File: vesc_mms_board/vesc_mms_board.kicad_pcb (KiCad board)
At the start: 2 copper layers, 60 x 104.5 mm, 51 parts, among them J1 RJ45_LED_Shielded, J2 RJ45_LED_Shielded, J3 Conn_01x04, J4 Conn_01x05, J5 VCC_IN, J6 Conn_01x02, SW1 SW_DIP_x02, U1 CH334R, Y1 12Mhz

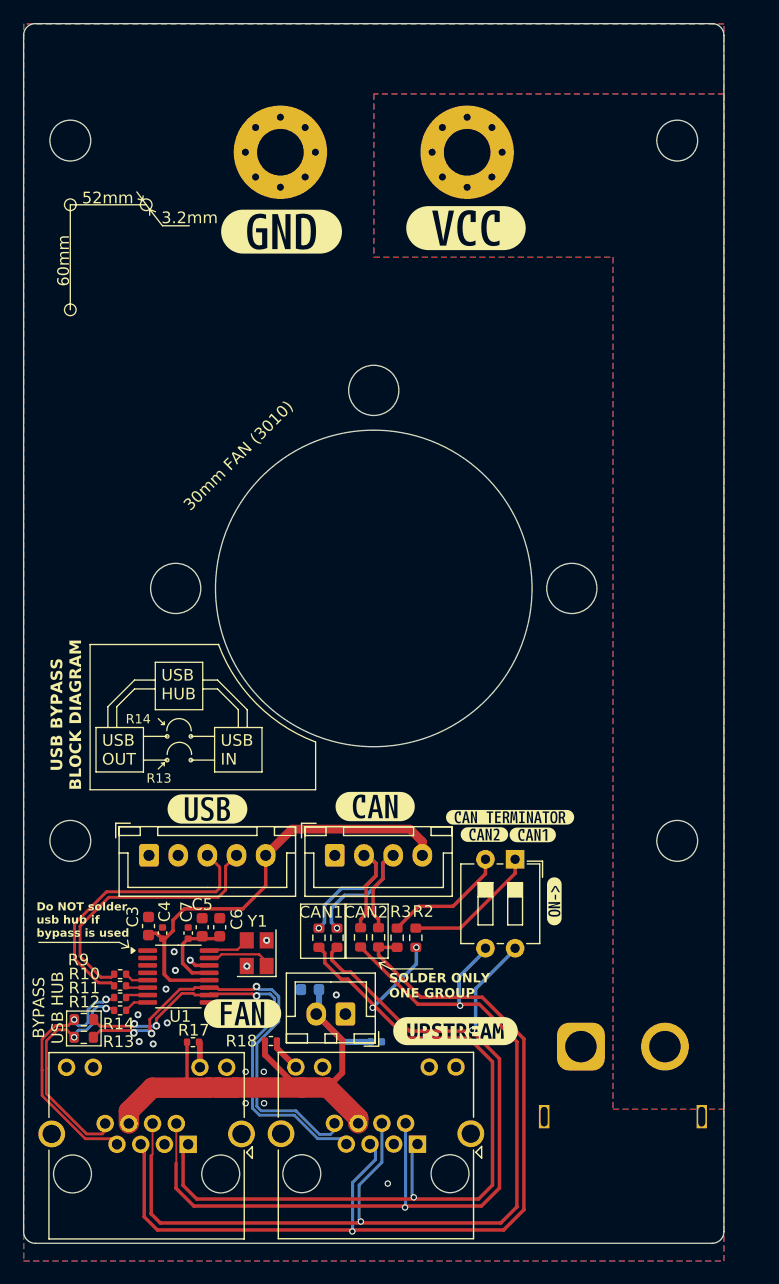
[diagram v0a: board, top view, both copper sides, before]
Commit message: fixed xt60 connvetor
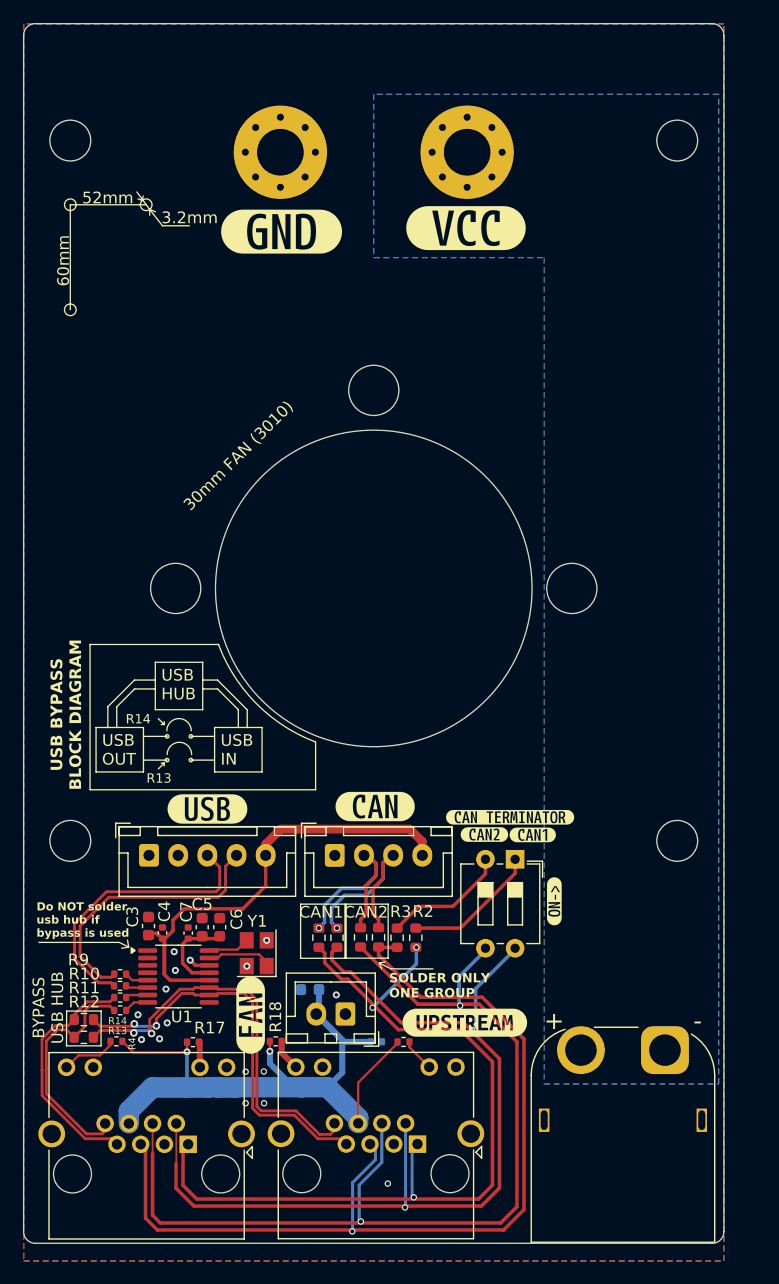
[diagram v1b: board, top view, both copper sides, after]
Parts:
- added R1: 1k, Resistor_SMD:R_0402_1005Metric, F.Cu at (112.5, 131.2)
- added R4: 1k, Resistor_SMD:R_0402_1005Metric, F.Cu at (88.0, 131.2)
- J5: moved to F.Cu
- moved J5 7.21 mm to (134.9, 131.9), turned to 180 degrees
- moved kibuzzard-6754762D 1.08 mm to (117.8, 129.6)
- moved kibuzzard-674E4631 0.70 mm to (99.5, 128.9), turned to 90 degrees
- moved R18 0.41 mm to (101.6, 131.2)
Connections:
- J1 pad 10: unconnected-(J1-Pad10) -> Net-(J1-Pad10)
- J1 pad 9: unconnected-(J1-Pad9) -> GND
- J2 pad 11: unconnected-(J2-Pad11) -> GND
- J2 pad 12: unconnected-(J2-Pad12) -> Net-(J2-Pad12)
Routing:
- net +12V: track 48.1 -> 62.3 mm, vias 0 -> 2
- net Net-(J2-Pad12): track 0.00 -> 4.87 mm
- net USB_UPSTREAM_D+: track 38.1 -> 35.0 mm, vias 3 -> 2
- net USB_UPSTREAM_D-: track 37.3 -> 34.4 mm, vias 3 -> 2
- net Net-(J1-Pad10): track 0.00 -> 2.75 mm
- net USB_DOWNSTREAM_D-: track 21.8 -> 21.1 mm, vias 2 -> 0
- net +5V: track 41.8 -> 42.3 mm
- net USB_DOWNSTREAM_D+: track 20.0 -> 20.5 mm, vias 2 -> 0
- removed copper zone on F.Cu, net VCC

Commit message: added gerber files
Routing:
- net GND: vias 16 -> 404

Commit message: added gerber files
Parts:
- C1, C2: moved to F.Cu
- moved R1 11.7 mm to (101.2, 128.8), turned to -90 degrees
- moved C2 10.2 mm to (103.0, 123.9), turned to -90 degrees
- moved C1 4.37 mm to (101.8, 123.3), turned to -90 degrees
- moved Y1 0.68 mm to (99.3, 123.6)
- moved R18 0.65 mm to (101.1, 130.7), turned to 90 degrees
- moved J6 0.44 mm to (107.1, 128.8)
- moved kibuzzard-674E4620 0.17 mm to (95.7, 111.1)
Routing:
- net Net-(J1-Pad10): track 2.75 -> 15.3 mm
- net +12V: track 62.3 -> 56.5 mm
- net GND: track 2.23 -> 5.71 mm, vias 404 -> 358
- net Net-(J1-Pad12): track 2.70 -> 4.16 mm
- net Net-(U1-XI): track 3.59 -> 2.93 mm
- net Net-(U1-XO): track 5.67 -> 5.12 mm
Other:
- board size 60 x 104.5 mm -> 60 x 99.7 mm
- board text added: "Voltage rating 12-60V"
- board text removed: "Voltage rating 12-50V"
